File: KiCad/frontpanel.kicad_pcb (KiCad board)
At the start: 2 copper layers, 139.7 x 88.9 mm, 26 parts, among them P1 CONN_02X13, P2 CONN_02X13

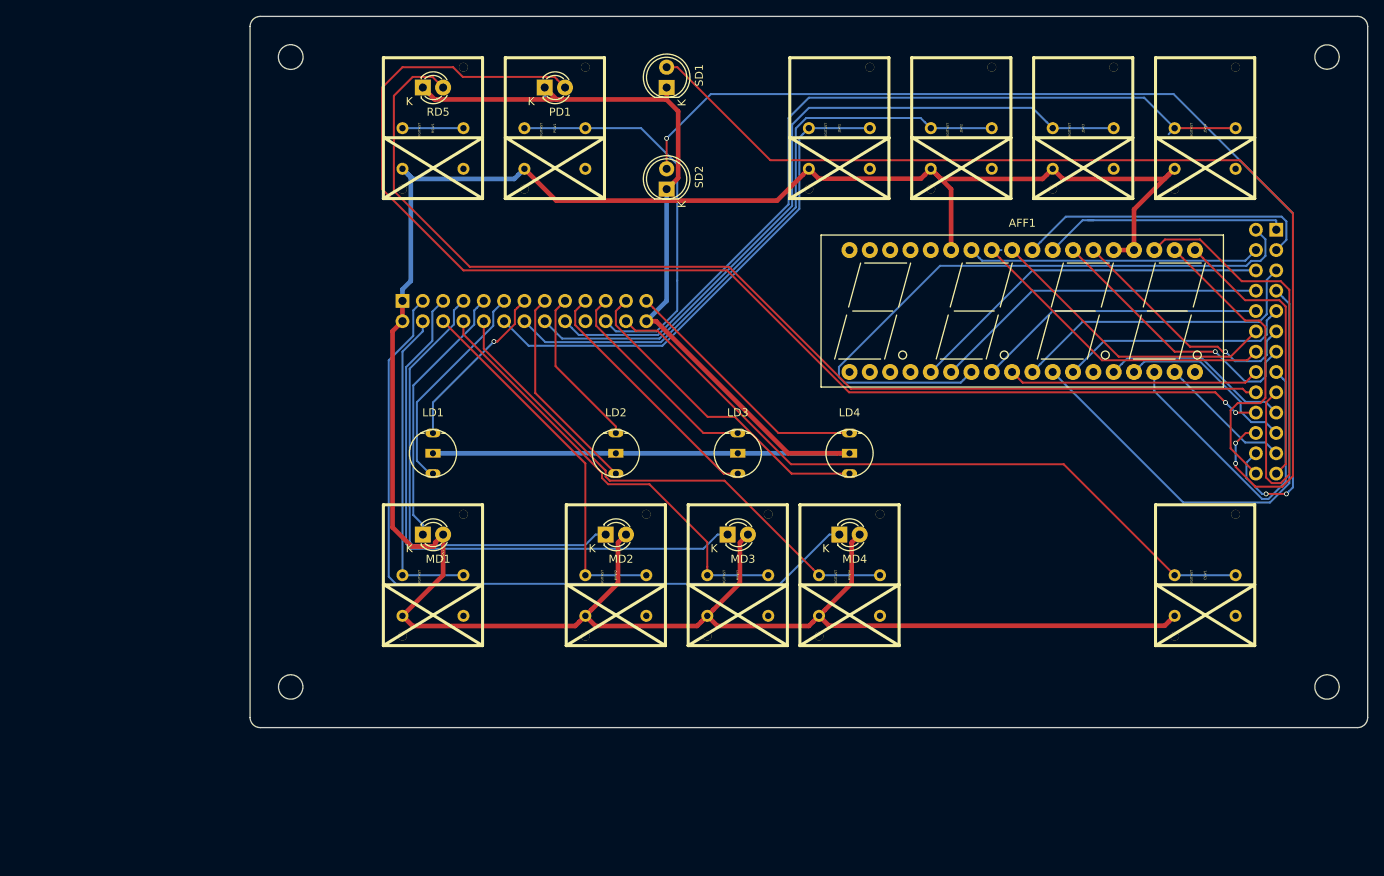
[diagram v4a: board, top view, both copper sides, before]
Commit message: adjusted frontpanel board size
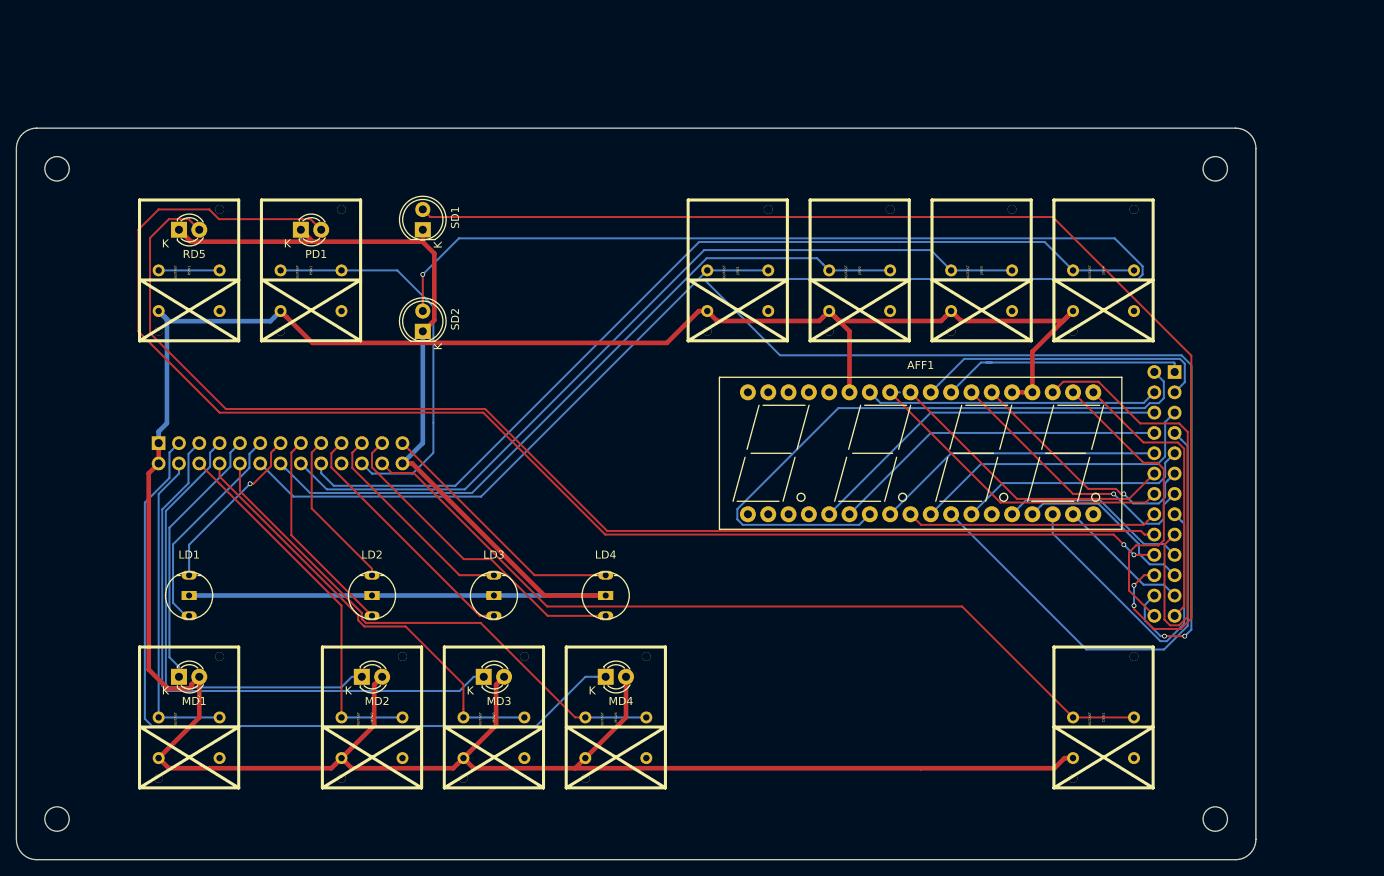
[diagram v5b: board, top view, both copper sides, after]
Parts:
- moved SD1 35.3 mm to (119.4, 63.5)
- moved SD2 35.3 mm to (119.4, 76.2)
- moved LD1 35.3 mm to (90.2, 109.2)
- moved MD2 35.3 mm to (111.8, 119.4)
- moved P1 35.3 mm to (86.4, 90.2)
- moved PD1 35.3 mm to (104.1, 63.5)
- moved RSW1 35.3 mm to (90.2, 68.6)
- moved LD2 35.3 mm to (113.0, 109.2)
- moved LD3 35.3 mm to (128.3, 109.2)
- moved LD4 35.3 mm to (142.2, 109.2)
- moved MD1 35.3 mm to (88.9, 119.4)
- moved MD3 35.3 mm to (127.0, 119.4)
- moved MSW1 35.3 mm to (90.2, 124.5)
- moved PSW1 35.3 mm to (105.4, 68.6)
- moved RD5 35.3 mm to (88.9, 63.5)
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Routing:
- net Net-(P2-Pad24): track 135.4 -> 263.0 mm
- net Net-(AFF1-Pad22): track 334.1 -> 370.4 mm
- net Net-(P2-Pad22): track 133.5 -> 151.3 mm
- net Net-(CSW1-Pad0): track 89.4 -> 107.1 mm
- net Net-(P2-Pad20): track 158.5 -> 176.2 mm
- net Net-(P2-Pad18): track 137.8 -> 155.5 mm
- net Net-(JSW2-Pad0): track 77.4 -> 91.5 mm
- net Net-(JSW1-Pad0): track 63.5 -> 76.9 mm
- net Net-(JSW3-Pad0): track 91.0 -> 103.7 mm
- net Net-(JSW4-Pad0): track 105.8 -> 117.6 mm
- net Net-(MD4-Pad1): track 95.5 -> 96.8 mm
- net Net-(MSW4-Pad0): track 65.1 -> 66.4 mm
- net (no net): track 1.27 -> 2.54 mm
- net Net-(AFF1-Pad11): track 62.1 -> 62.6 mm
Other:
- board size 139.7 x 88.9 mm -> 154.9 x 91.4 mm
